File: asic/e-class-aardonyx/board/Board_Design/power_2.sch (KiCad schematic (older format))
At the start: 52 parts, among them Q1 FDN339AN, SW2 FSM2JSMAATR, U10 TPS7A7002DDAR, U11 ADM1186, U13 TPS7A7002DDAR, U14 74AUP1G09GW

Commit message: Layout update
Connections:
- net V3P3: now also R140.1
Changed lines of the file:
@@
 	0    1    1    0
 $EndComp
-Wire Wire Line
-	5250 6800 5150 6800
 $Comp
 L Aardonyx-rescue:R_US-aardonyx R?
@@
 	5100 6450 5600 6450
 Wire Wire Line
-	5600 7150 5600 6450
+	5600 7150 5600 6800
 Wire Wire Line
 	5150 7150 5600 7150
@@
 	0    1    1    0
 $EndComp
+Wire Wire Line
+	5150 6800 5600 6800
+Connection ~ 5600 6800
+Wire Wire Line
+	5600 6800 5600 6450
 $EndSCHEMATC

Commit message: Updating layout
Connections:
- net GND: now also U10.9 (PGND), U13.9 (PGND)
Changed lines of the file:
@@
 	3000 2050 3000 2100
 Wire Wire Line
-	2300 2500 2300 2600
+	2300 2500 2300 2550
 Wire Wire Line
 	3650 1650 3650 1800
@@
 	8800 1850 9200 1850
 Wire Wire Line
-	7300 2700 7300 2800
+	7300 2700 7300 2750
 Wire Wire Line
 	8000 2250 8000 2300
@@
 Wire Wire Line
 	5600 6800 5600 6450
+Wire Wire Line
+	2400 2500 2400 2550
+Wire Wire Line
+	2400 2550 2300 2550
+Connection ~ 2300 2550
+Wire Wire Line
+	2300 2550 2300 2600
+Wire Wire Line
+	7400 2700 7400 2750
+Wire Wire Line
+	7400 2750 7300 2750
+Connection ~ 7300 2750
+Wire Wire Line
+	7300 2750 7300 2800
 $EndSCHEMATC

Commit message: Updating layout
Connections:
- net GND: now also U10.1 (NC), U13.1 (NC)
- net V5P0: now also U10.4 (NC), U13.4 (NC)
- net at C56.1, P_R1.2, P_R41.1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: now also U10.5 (NC)
- net at C62.1, P_R2.2, P_R49.1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: now also U13.5 (NC)
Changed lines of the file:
@@
 Text Notes 2000 900  0    100  ~ 20
 5V TO 3.3V LDO
-$Comp
-L Aardonyx-rescue:TPS7A7002DDAR-aardonyx U10
-U 1 1 5EC15037
-P 2300 1950
-F 0 "U10" H 2300 2565 50  0000 C CNN
-F 1 "TPS7A7002DDAR" H 2300 2474 50  0000 C CNN
-F 2 "Package_SO:SOIC-8-1EP_3.9x4.9mm_P1.27mm_EP2.29x3mm_ThermalVias" H 2300 1950 50  0001 C CNN
-F 3 "https://www.digikey.in/product-detail/en/texas-instruments/TPS7A7002DDAR/296-40977-1-ND/5178854" H 2300 1950 50  0001 C CNN
-F 4 "IC REG LIN POS ADJ 3A 8SO PWRPAD" H 2300 1950 50  0001 C CNN "Description"
-F 5 "296-40977-1-ND" H 2300 1950 50  0001 C CNN "Digikey PartNumber"
-F 6 "TPS7A7002DDAR" H 2300 1950 50  0001 C CNN "Manufactured Part Number"
-F 7 "Texas Instruments" H 2300 1950 50  0001 C CNN "Maufaturer"
-	1    2300 1950
-	1    0    0    -1
-$EndComp
-Wire Wire Line
-	2750 1650 3000 1650
+Wire Wire Line
+	2750 1650 2900 1650
 Wire Wire Line
 	3000 1650 3000 1700
@@
 	1300 1600 1300 1650
 Wire Wire Line
-	1650 1350 1650 1850
-Wire Wire Line
-	6650 1550 6650 2050
+	6650 1550 6650 1850
 Wire Wire Line
 	6300 1800 6300 1850
@@
 Wire Wire Line
 	8000 1850 8000 1900
-Wire Wire Line
-	7750 1850 8000 1850
 $Comp
 L Aardonyx-rescue:TPS7A7002DDAR-aardonyx U13
@@
 Wire Wire Line
 	7300 2750 7300 2800
+Wire Wire Line
+	1650 1350 1650 1650
+$Comp
+L Aardonyx-rescue:TPS7A7002DDAR-aardonyx U10
+U 1 1 5EC15037
+P 2300 1950
+F 0 "U10" H 2300 2565 50  0000 C CNN
+F 1 "TPS7A7002DDAR" H 2300 2474 50  0000 C CNN
+F 2 "Package_SO:SOIC-8-1EP_3.9x4.9mm_P1.27mm_EP2.29x3mm_ThermalVias" H 2300 1950 50  0001 C CNN
+F 3 "https://www.digikey.in/product-detail/en/texas-instruments/TPS7A7002DDAR/296-40977-1-ND/5178854" H 2300 1950 50  0001 C CNN
+F 4 "IC REG LIN POS ADJ 3A 8SO PWRPAD" H 2300 1950 50  0001 C CNN "Description"
+F 5 "296-40977-1-ND" H 2300 1950 50  0001 C CNN "Digikey PartNumber"
+F 6 "TPS7A7002DDAR" H 2300 1950 50  0001 C CNN "Manufactured Part Number"
+F 7 "Texas Instruments" H 2300 1950 50  0001 C CNN "Maufaturer"
+	1    2300 1950
+	1    0    0    -1
+$EndComp
+Wire Wire Line
+	1650 1650 1850 1650
+Connection ~ 1650 1650
+Wire Wire Line
+	1650 1650 1650 1850
+Wire Wire Line
+	1850 2250 1700 2250
+Wire Wire Line
+	1700 2250 1700 2550
+Wire Wire Line
+	1700 2550 2300 2550
+Wire Wire Line
+	2750 1800 2900 1800
+Wire Wire Line
+	2900 1800 2900 1650
+Connection ~ 2900 1650
+Wire Wire Line
+	2900 1650 3000 1650
+Wire Wire Line
+	7750 2000 7850 2000
+Wire Wire Line
+	7850 2000 7850 1850
+Wire Wire Line
+	7750 1850 7850 1850
+Connection ~ 7850 1850
+Wire Wire Line
+	7850 1850 8000 1850
+Wire Wire Line
+	7300 2750 6700 2750
+Wire Wire Line
+	6700 2750 6700 2450
+Wire Wire Line
+	6700 2450 6850 2450
+Wire Wire Line
+	6850 1850 6650 1850
+Connection ~ 6650 1850
+Wire Wire Line
+	6650 1850 6650 2050
+Connection ~ 9700 2450
 $EndSCHEMATC

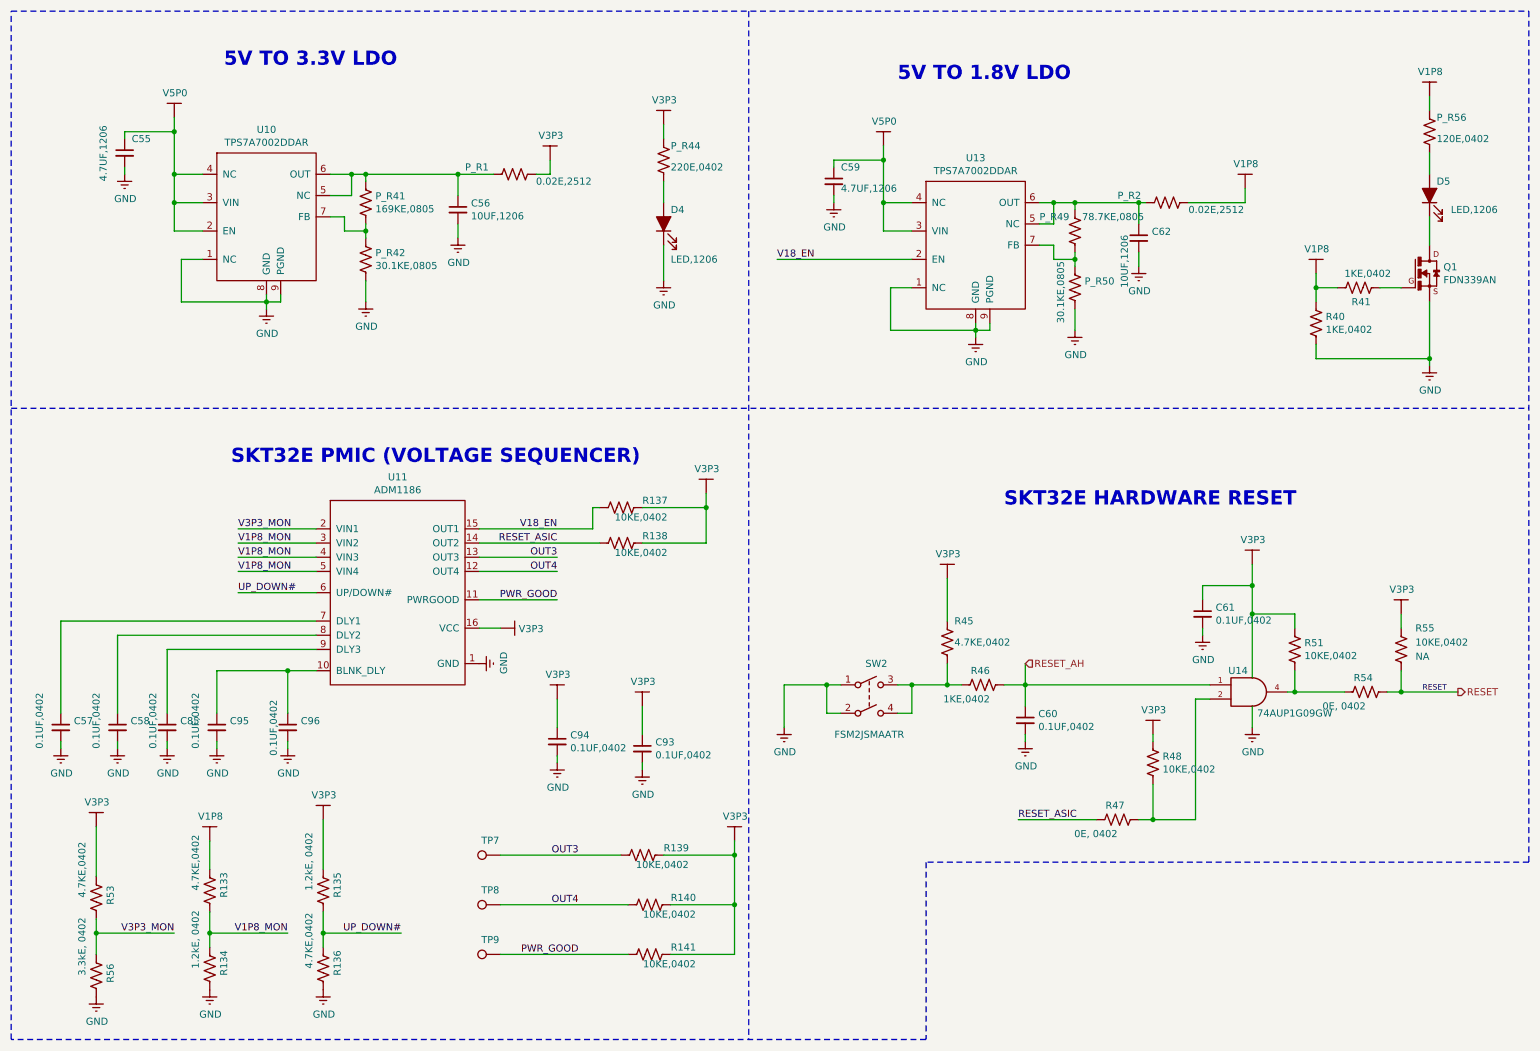
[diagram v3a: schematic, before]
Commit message: Updating layout after back annotation
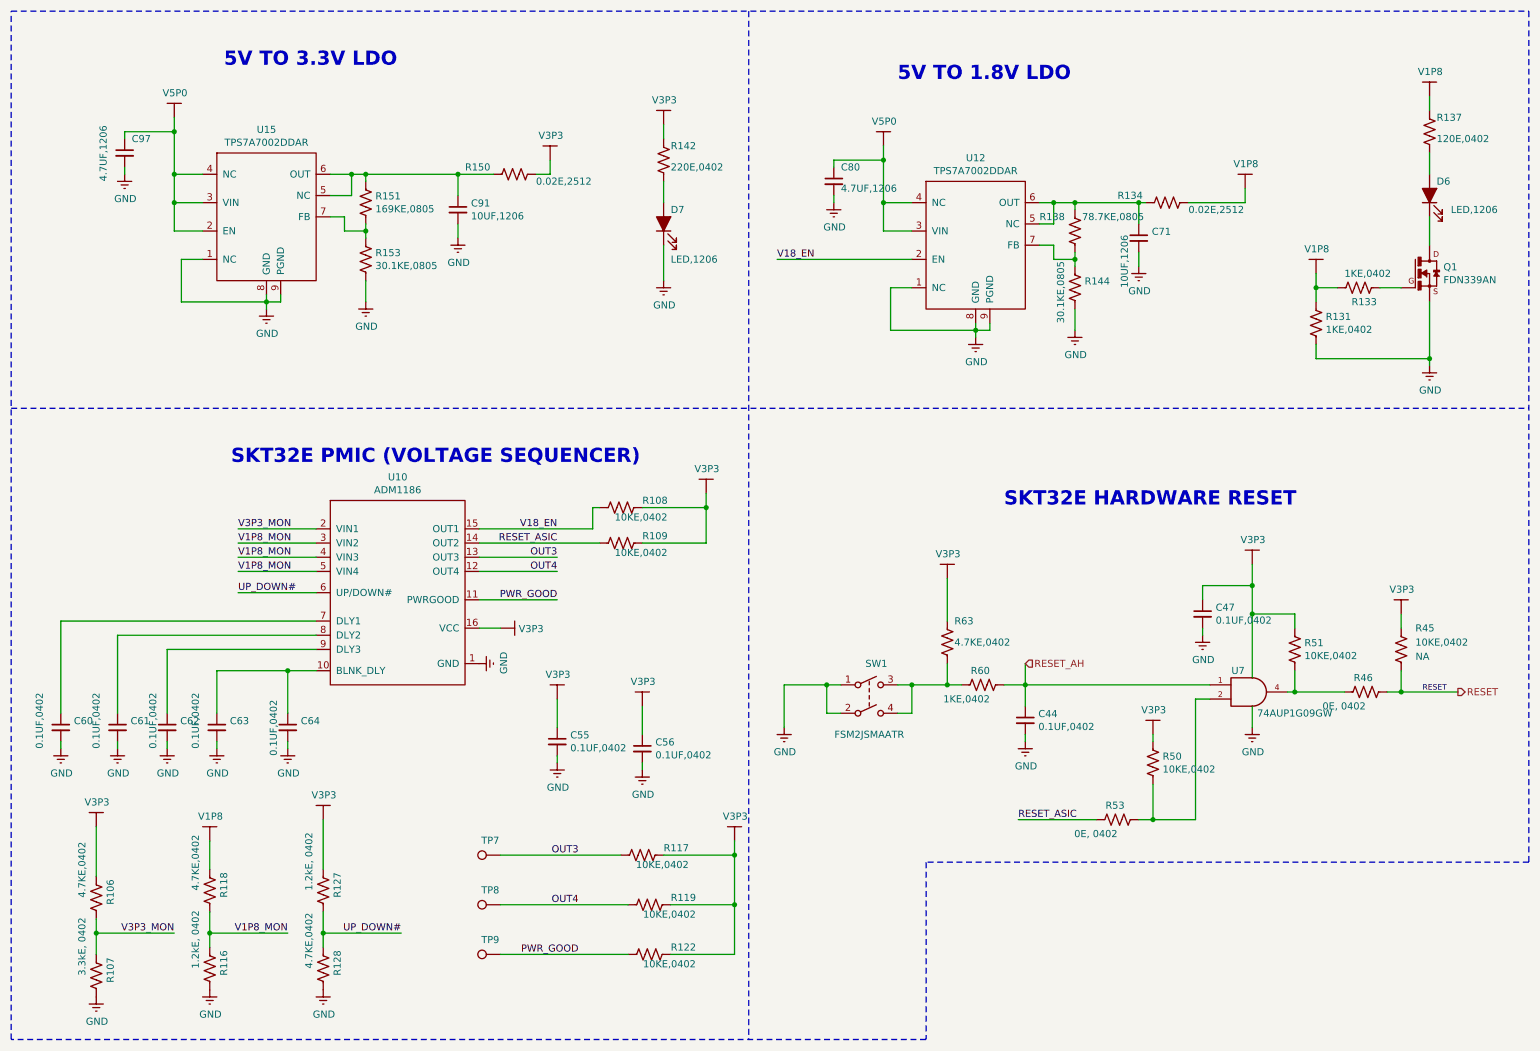
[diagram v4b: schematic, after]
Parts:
- renumbered C60 to C44, C61 to C47, C94 to C55, C93 to C56, C57 to C60, C58 to C61, C85 to C62, C95 to C63, C96 to C64, C62 to C71, C59 to C80, C56 to C91, C55 to C97, D5 to D6, D4 to D7, R53 to R106, R56 to R107, R137 to R108, R138 to R109, R134 to R116, R139 to R117, R133 to R118, R140 to R119, R141 to R122, R135 to R127, R136 to R128, R40 to R131, R41 to R133, P_R2 to R134, P_R56 to R137, P_R49 to R138, P_R44 to R142, P_R50 to R144, P_R1 to R150, P_R41 to R151, P_R42 to R153, R55 to R45, R54 to R46, R48 to R50, R47 to R53, R46 to R60, R45 to R63, SW2 to SW1, U11 to U10, U13 to U12, U10 to U15
